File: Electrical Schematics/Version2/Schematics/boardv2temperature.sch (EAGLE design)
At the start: 12 parts

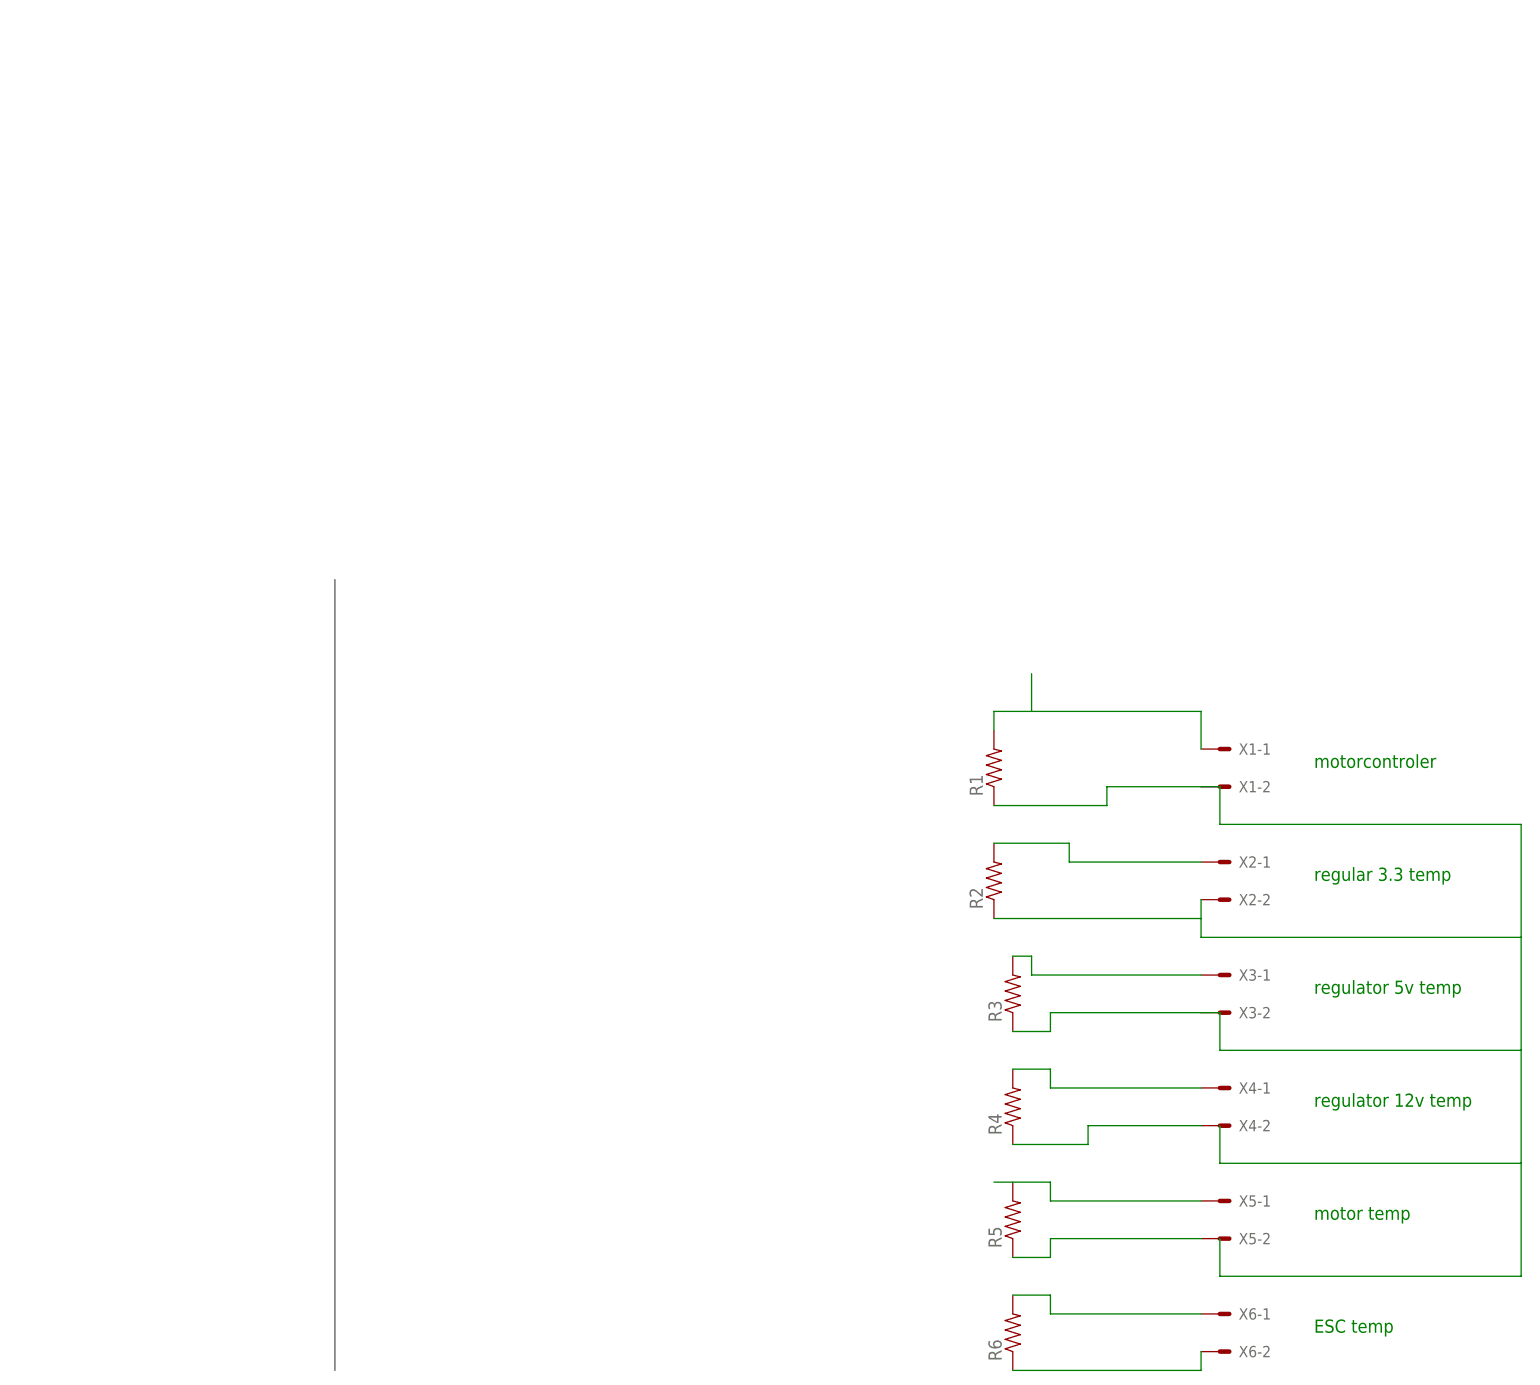
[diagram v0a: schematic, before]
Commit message: updated the schematics for the ridgley
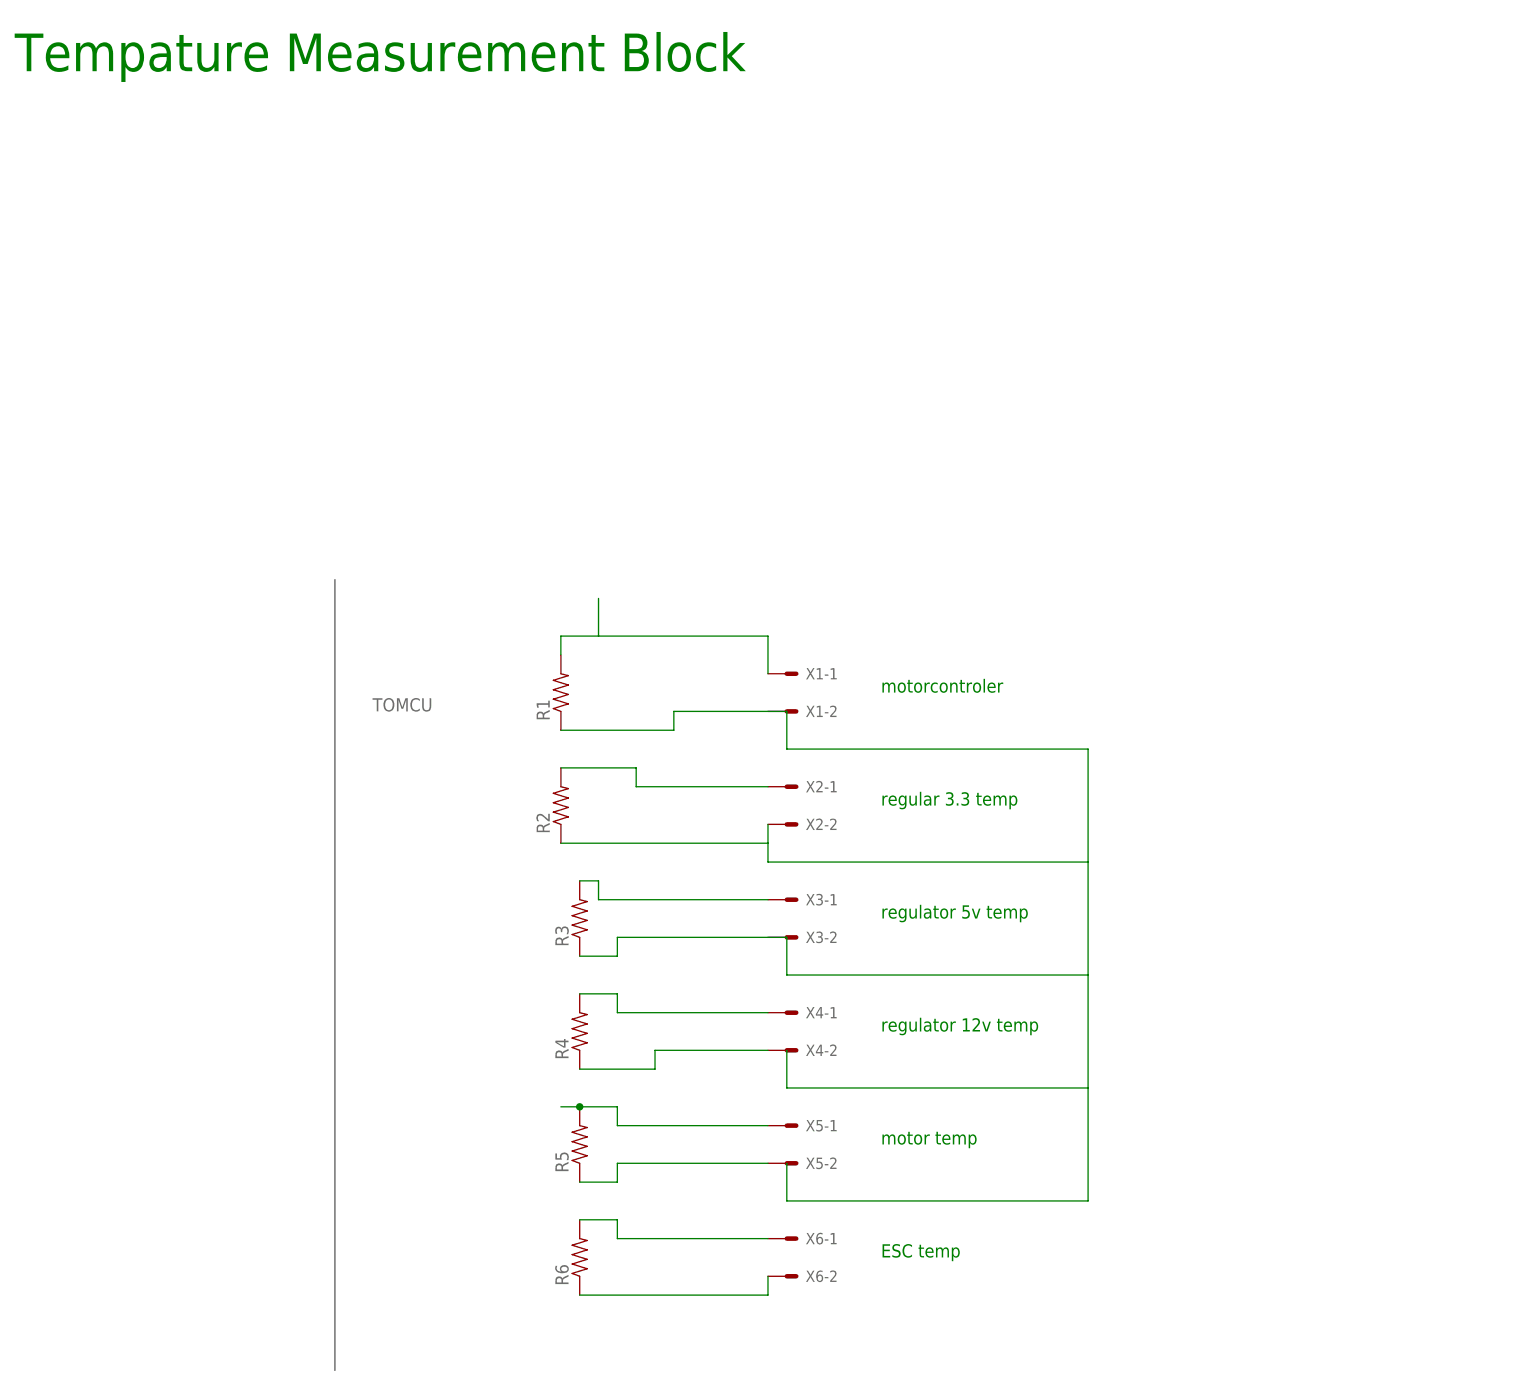
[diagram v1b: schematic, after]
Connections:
- net N$5: now also R5.2
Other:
- note added: "Tempature Measurement Block"
- moved on the sheet: R1, R2, R3, R4, R5, R6, X1-1, X1-2, X2-1, X2-2, X3-1, X3-2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

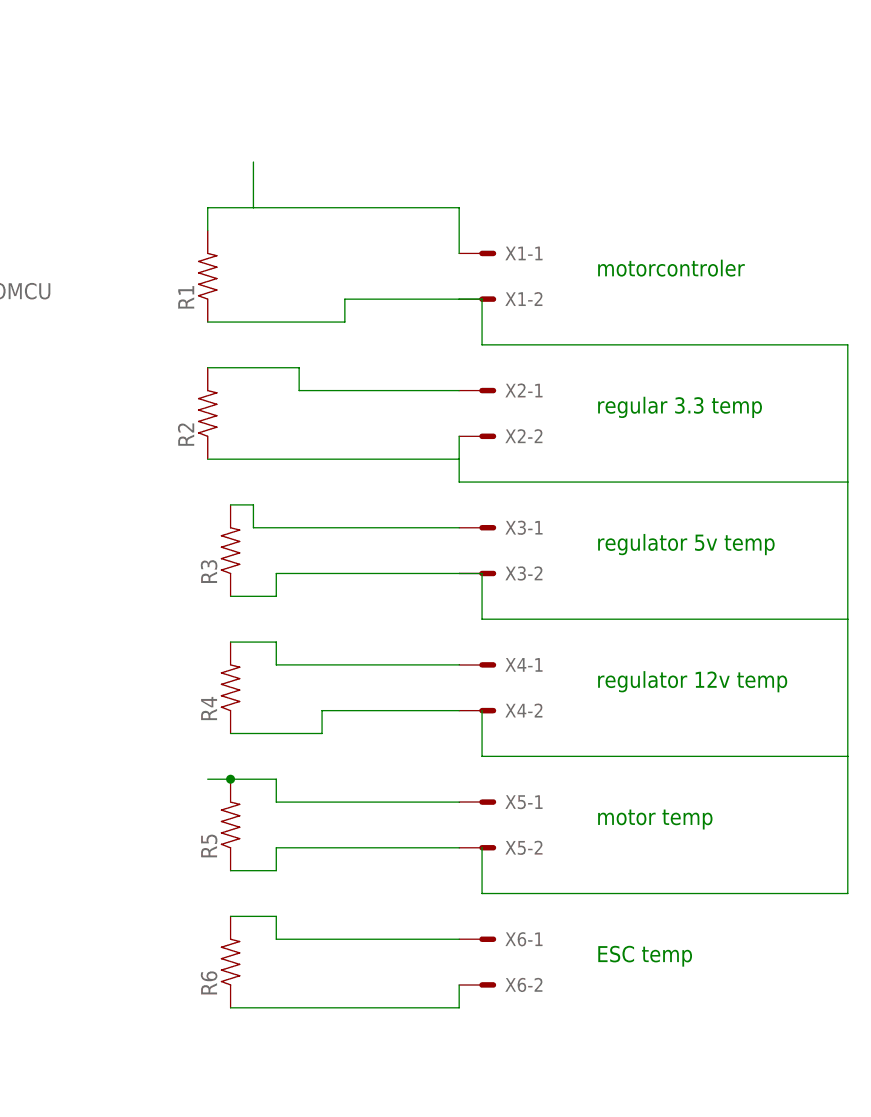
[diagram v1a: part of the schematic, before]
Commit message: Fixed Temperature Sensors
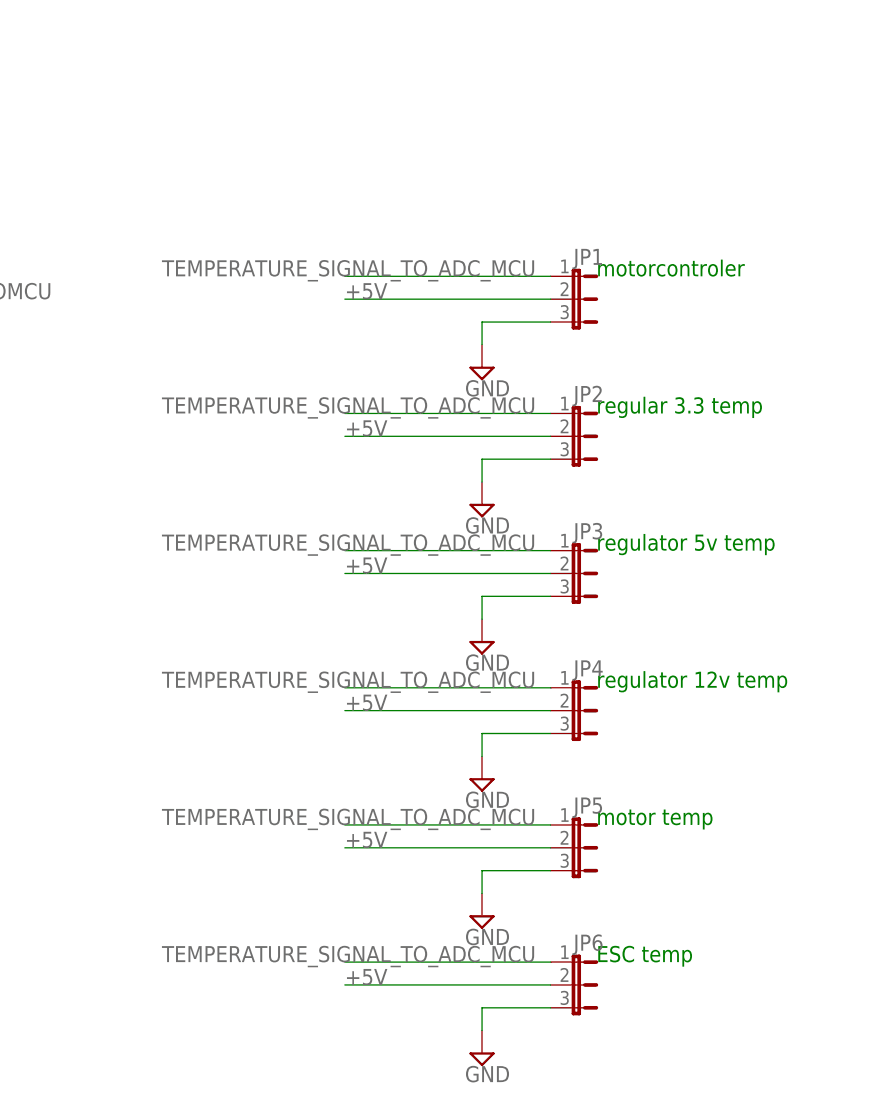
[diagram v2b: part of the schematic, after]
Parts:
- removed R1, R2, R3, R4, R5, R6: (no value), SparkFun-Passives:RESISTOR0603-RES
- removed X1, X2, X3, X4, X5, X6: (no value), con-molex:KK-156-2
- added JP1, JP2, JP3, JP4, JP5, JP6: (no value), jumper:JP2E
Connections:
- removed net N$1: R1.2, X1-1.S
- removed net N$10: R4.1, X4-2.S
- removed net N$11: R5.1, X5-2.S
- removed net N$12: R6.1, X6-2.S
- removed net N$2: R2.2, X2-1.S
- removed net N$3: R3.2, X3-1.S
- removed net N$4: R4.2, X4-1.S
- removed net N$5: R5.2, X5-1.S
- removed net N$6: R6.2, X6-1.S
- removed net N$8: R1.1, R2.1, R3.1, X1-2.S, X2-2.S, X3-2.S
- new net +5V: JP1.2, JP2.2, JP3.2, JP4.2, JP5.2, JP6.2
- new net GND: JP1.3, JP2.3, JP3.3, JP4.3, JP5.3, JP6.3
- new net TEMPERATURE_SIGNAL_TO_ADC_MCU: JP1.1, JP2.1, JP3.1, JP4.1, JP5.1, JP6.1

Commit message: updated temp
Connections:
- net +5V renamed 3.3V_TEMP_PWR
- removed net TEMPERATURE_SIGNAL_TO_ADC_MCU: JP1.1, JP2.1, JP3.1, JP4.1, JP5.1, JP6.1
- new net MCU_TEMPB_A1: JP2.1
- new net MCU_TEMPC_A2: JP3.1
- new net MCU_TEMPD_A4: JP4.1
- new net MCU_TEMPE_A5: JP5.1
- new net MCU_TEMPF_A6: JP6.1
- new net MCU_TEMP_A0: JP1.1
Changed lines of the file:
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@@
 </instances>
 <busses>
-<bus name="TOMCU">
-<segment>
-<wire x1="-27.94" y1="114.3" x2="-27.94" y2="7.62" width="0.762" layer="92"/>
-<label x="-22.86" y="96.52" size="1.778" layer="95"/>
-</segment>
-</bus>
 </busses>
 <nets>
-<net name="TEMPERATURE_SIGNAL_TO_ADC_MCU" class="0">
-<segment>
-<pinref part="JP1" gate="1" pin="1"/>
-<wire x1="40.64" y1="99.06" x2="17.78" y2="99.06" width="0.1524" layer="91"/>
-<label x="-2.54" y="99.06" size="1.778" layer="95"/>
-</segment>
-<segment>
-<pinref part="JP2" gate="1" pin="1"/>
-<wire x1="40.64" y1="83.82" x2="17.78" y2="83.82" width="0.1524" layer="91"/>
-<label x="-2.54" y="83.82" size="1.778" layer="95"/>
-</segment>
-<segment>
-<pinref part="JP3" gate="1" pin="1"/>
-<wire x1="40.64" y1="68.58" x2="17.78" y2="68.58" width="0.1524" layer="91"/>
-<label x="-2.54" y="68.58" size="1.778" layer="95"/>
-</segment>
-<segment>
-<pinref part="JP4" gate="1" pin="1"/>
-<wire x1="40.64" y1="53.34" x2="17.78" y2="53.34" width="0.1524" layer="91"/>
-<label x="-2.54" y="53.34" size="1.778" layer="95"/>
-</segment>
-<segment>
-<pinref part="JP5" gate="1" pin="1"/>
-<wire x1="40.64" y1="38.1" x2="17.78" y2="38.1" width="0.1524" layer="91"/>
-<label x="-2.54" y="38.1" size="1.778" layer="95"/>
-</segment>
+<net name="MCU_TEMPF_A6" class="0">
 <segment>
 <pinref part="JP6" gate="1" pin="1"/>
 <wire x1="40.64" y1="22.86" x2="17.78" y2="22.86" width="0.1524" layer="91"/>
-<label x="-2.54" y="22.86" size="1.778" layer="95"/>
-</segment>
-</net>
-<net name="+5V" class="0">
-<segment>
-<pinref part="JP1" gate="1" pin="2"/>
-<wire x1="40.64" y1="96.52" x2="17.78" y2="96.52" width="0.1524" layer="91"/>
-<label x="17.78" y="96.52" size="1.778" layer="95"/>
-</segment>
-<segment>
-<pinref part="JP2" gate="1" pin="2"/>
-<wire x1="40.64" y1="81.28" x2="17.78" y2="81.28" width="0.1524" layer="91"/>
-<label x="17.78" y="81.28" size="1.778" layer="95"/>
-</segment>
-<segment>
-<pinref part="JP3" gate="1" pin="2"/>
-<wire x1="40.64" y1="66.04" x2="17.78" y2="66.04" width="0.1524" layer="91"/>
-<label x="17.78" y="66.04" size="1.778" layer="95"/>
-</segment>
-<segment>
-<pinref part="JP4" gate="1" pin="2"/>
-<wire x1="40.64" y1="50.8" x2="17.78" y2="50.8" width="0.1524" layer="91"/>
-<label x="17.78" y="50.8" size="1.778" layer="95"/>
-</segment>
-<segment>
-<pinref part="JP5" gate="1" pin="2"/>
-<wire x1="40.64" y1="35.56" x2="17.78" y2="35.56" width="0.1524" layer="91"/>
-<label x="17.78" y="35.56" size="1.778" layer="95"/>
-</segment>
-<segment>
-<pinref part="JP6" gate="1" pin="2"/>
-<wire x1="40.64" y1="20.32" x2="17.78" y2="20.32" width="0.1524" layer="91"/>
-<label x="17.78" y="20.32" size="1.778" layer="95"/>
+<label x="17.78" y="22.86" size="1.778" layer="95" rot="R180" xref="yes"/>
 </segment>
 </net>
@@
 </segment>
 </net>
+<net name="MCU_TEMP_A0" class="0">
+<segment>
+<pinref part="JP1" gate="1" pin="1"/>
+<wire x1="40.64" y1="99.06" x2="17.78" y2="99.06" width="0.1524" layer="91"/>
+<label x="17.78" y="99.06" size="1.778" layer="95" rot="R180" xref="yes"/>
+</segment>
+</net>
+<net name="MCU_TEMPB_A1" class="0">
+<segment>
+<pinref part="JP2" gate="1" pin="1"/>
+<wire x1="40.64" y1="83.82" x2="17.78" y2="83.82" width="0.1524" layer="91"/>
+<label x="17.78" y="83.82" size="1.778" layer="95" rot="R180" xref="yes"/>
+</segment>
+</net>
+<net name="MCU_TEMPC_A2" class="0">
+<segment>
+<pinref part="JP3" gate="1" pin="1"/>
+<wire x1="40.64" y1="68.58" x2="17.78" y2="68.58" width="0.1524" layer="91"/>
+<label x="17.78" y="68.58" size="1.778" layer="95" rot="R180" xref="yes"/>
+</segment>
+</net>
+<net name="MCU_TEMPD_A4" class="0">
+<segment>
+<pinref part="JP4" gate="1" pin="1"/>
+<wire x1="40.64" y1="53.34" x2="17.78" y2="53.34" width="0.1524" layer="91"/>
+<label x="17.78" y="53.34" size="1.778" layer="95" rot="R180" xref="yes"/>
+</segment>
+</net>
+<net name="MCU_TEMPE_A5" class="0">
+<segment>
+<pinref part="JP5" gate="1" pin="1"/>
+<wire x1="40.64" y1="38.1" x2="17.78" y2="38.1" width="0.1524" layer="91"/>
+<label x="17.78" y="38.1" size="1.778" layer="95" rot="R180" xref="yes"/>
+</segment>
+</net>
+<net name="3.3V_TEMP_PWR" class="0">
+<segment>
+<pinref part="JP1" gate="1" pin="2"/>
+<wire x1="40.64" y1="96.52" x2="17.78" y2="96.52" width="0.1524" layer="91"/>
+<label x="17.78" y="93.98" size="1.778" layer="95" rot="R180" xref="yes"/>
+<wire x1="17.78" y1="96.52" x2="17.78" y2="93.98" width="0.1524" layer="91"/>
+</segment>
+<segment>
+<pinref part="JP2" gate="1" pin="2"/>
+<wire x1="40.64" y1="81.28" x2="17.78" y2="81.28" width="0.1524" layer="91"/>
+<label x="17.78" y="78.74" size="1.778" layer="95" rot="R180" xref="yes"/>
+</segment>
+<segment>
+<pinref part="JP3" gate="1" pin="2"/>
+<wire x1="40.64" y1="66.04" x2="17.78" y2="66.04" width="0.1524" layer="91"/>
+<label x="17.78" y="63.5" size="1.778" layer="95" rot="R180" xref="yes"/>
+<wire x1="17.78" y1="66.04" x2="17.78" y2="63.5" width="0.1524" layer="91"/>
+</segment>
+<segment>
+<pinref part="JP5" gate="1" pin="2"/>
+<wire x1="40.64" y1="35.56" x2="17.78" y2="35.56" width="0.1524" layer="91"/>
+<label x="17.78" y="33.02" size="1.778" layer="95" rot="R180" xref="yes"/>
+<wire x1="17.78" y1="35.56" x2="17.78" y2="33.02" width="0.1524" layer="91"/>
+</segment>
+<segment>
+<pinref part="JP4" gate="1" pin="2"/>
+<wire x1="40.64" y1="50.8" x2="17.78" y2="50.8" width="0.1524" layer="91"/>
+<label x="17.78" y="48.26" size="1.778" layer="95" rot="R180" xref="yes"/>
+<wire x1="17.78" y1="50.8" x2="17.78" y2="48.26" width="0.1524" layer="91"/>
+</segment>
+<segment>
+<pinref part="JP6" gate="1" pin="2"/>
+<wire x1="40.64" y1="20.32" x2="17.78" y2="20.32" width="0.1524" layer="91"/>
+<label x="17.78" y="17.78" size="1.778" layer="95" rot="R180" xref="yes"/>
+<wire x1="17.78" y1="20.32" x2="17.78" y2="17.78" width="0.1524" layer="91"/>
+</segment>
+</net>
